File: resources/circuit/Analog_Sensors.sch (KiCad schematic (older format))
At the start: 43 parts, among them J3 Screw_Terminal_1x08, Q10 BSS138, Q11 BSS138, Q7 BSS138, Q8 BSS138, Q9 BSS138, U13 Airspeed, U14 Static Pressure, U15 MAP Pressure, U16 MCP3008, U8 MCP3008

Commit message: Schematic work
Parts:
- removed U16: MCP3008, SMD_Packages:SO-16-L, symbol MCP3008
- added U9: MCP3008, symbol MCP3008
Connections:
- net +5V: now also U9.15 (VREF), U9.16 (VDD)
- net ASI: now also U8.1 (CH0)
- net BARO: now also U8.2 (CH1)
- net CHT: now also U8.6 (CH5)
- net CurrentMeter: now also U8.7 (CH6)
- net GND: now also U9.14 (AGND), U9.9 (DGND)
- net MAP: now also U8.3 (CH2)
- net MCP0H: now also U8.10 (~CS~/SHDN)
- net MCP1H: now also U9.10 (~CS~/SHDN); no longer U8.10 (~CS~/SHDN)
- net MISOH: now also U9.12 (DOUT)
- net MOSIH: now also U9.11 (DIN)
- net OilPressure: now also U8.4 (CH3)
- net OilTemp: now also U8.5 (CH4)
- net SCLKH: now also U9.13 (CLK)
- net VoltageMeter: now also U8.8 (CH7)
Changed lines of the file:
@@
 +5V
 $Comp
-L GND #PWR033
+L GND #PWR032
 U 1 1 5914E423
 P 5800 4610
-F 0 "#PWR033" H 5800 4610 30  0001 C CNN
+F 0 "#PWR032" H 5800 4610 30  0001 C CNN
 F 1 "GND" H 5800 4540 30  0001 C CNN
 F 2 "" H 5800 4610 60  0000 C CNN
@@
 $EndComp
 $Comp
-L GND #PWR034
+L GND #PWR033
 U 1 1 5914E429
 P 5800 2460
-F 0 "#PWR034" H 5800 2460 30  0001 C CNN
+F 0 "#PWR033" H 5800 2460 30  0001 C CNN
 F 1 "GND" H 5800 2390 30  0001 C CNN
 F 2 "" H 5800 2460 60  0000 C CNN
@@
 Text Label 4750 1260 2    60   ~ 0
 CHT
-$Comp
-L MCP3008 U16
-U 1 1 5914E457
-P 5800 1610
-F 0 "U16" H 5350 2060 50  0000 C CNN
-F 1 "MCP3008" H 6150 2060 50  0000 C CNN
-F 2 "SMD_Packages:SO-16-L" H 5700 1510 50  0001 C CNN
-F 3 "" H 5800 1610 50  0001 C CNN
-	1    5800 1610
-	1    0    0    -1
-$EndComp
 Text Notes 4970 5070 0    157  Italic 31
 A/D Module
@@
 $EndComp
 $Comp
-L GND #PWR035
+L GND #PWR034
 U 1 1 59151DCA
 P 1580 1450
-F 0 "#PWR035" H 1580 1450 30  0001 C CNN
+F 0 "#PWR034" H 1580 1450 30  0001 C CNN
 F 1 "GND" H 1580 1380 30  0001 C CNN
 F 2 "" H 1580 1450 60  0001 C CNN
@@
 $EndComp
 $Comp
-L GND #PWR036
+L GND #PWR035
 U 1 1 59151DFB
 P 1580 2450
-F 0 "#PWR036" H 1580 2450 30  0001 C CNN
+F 0 "#PWR035" H 1580 2450 30  0001 C CNN
 F 1 "GND" H 1580 2380 30  0001 C CNN
 F 2 "" H 1580 2450 60  0001 C CNN
@@
 $EndComp
 $Comp
-L GND #PWR037
+L GND #PWR036
 U 1 1 59151E25
 P 1580 3450
-F 0 "#PWR037" H 1580 3450 30  0001 C CNN
+F 0 "#PWR036" H 1580 3450 30  0001 C CNN
 F 1 "GND" H 1580 3380 30  0001 C CNN
 F 2 "" H 1580 3450 60  0001 C CNN
@@
 NoConn ~ 1830 5720
 NoConn ~ 1830 5920
-$Comp
-L MCP3008 U8
-U 1 1 59151B46
-P 5800 3760
-F 0 "U8" H 5350 4210 50  0000 C CNN
-F 1 "MCP3008" H 6150 4210 50  0000 C CNN
-F 2 "" H 5700 3660 50  0001 C CNN
-F 3 "" H 5800 3760 50  0001 C CNN
-	1    5800 3760
-	1    0    0    -1
-$EndComp
 Text HLabel 1800 6650 2    60   Input ~ 0
 +5V
@@
 $EndComp
 $Comp
-L GND #PWR038
+L GND #PWR037
 U 1 1 5915DC2B
 P 5590 6120
-F 0 "#PWR038" H 5590 6120 30  0001 C CNN
+F 0 "#PWR037" H 5590 6120 30  0001 C CNN
 F 1 "GND" H 5590 6050 30  0001 C CNN
 F 2 "" H 5590 6120 60  0001 C CNN
@@
 Wire Wire Line
 	4930 2010 4930 2250
+$Comp
+L MCP3008 U8
+U 1 1 59157E17
+P 5800 1610
+F 0 "U8" H 5350 2060 50  0000 C CNN
+F 1 "MCP3008" H 6150 2060 50  0000 C CNN
+F 2 "" H 5700 1510 50  0001 C CNN
+F 3 "" H 5800 1610 50  0001 C CNN
+	1    5800 1610
+	1    0    0    -1
+$EndComp
+$Comp
+L MCP3008 U9
+U 1 1 591584A5
+P 5800 3760
+F 0 "U9" H 5350 4210 50  0000 C CNN
+F 1 "MCP3008" H 6150 4210 50  0000 C CNN
+F 2 "" H 5700 3660 50  0001 C CNN
+F 3 "" H 5800 3760 50  0001 C CNN
+	1    5800 3760
+	1    0    0    -1
+$EndComp
 $EndSCHEMATC

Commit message: Another RPM reading solution
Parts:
- added C14, C?: 22n, symbol C_Small
- added D?: Diode, Diodes_SMD:D_0603, symbol D_Small
- added R14, R?: 47k, symbol R_Small
- added R15, R?: 100, symbol R_Small
- added R18, R? (x2): 100k, Resistors_SMD:R_0603, symbol R_Small
- added R19, R? (x3): 10k, Resistors_SMD:R_0603, symbol R_Small
- added R20, R?: 220, Resistors_SMD:R_0603, symbol R_Small
- added U10, U?: LTV-817, Housings_DIP:DIP-4_W7.62mm, symbol LTV-817
- added U11, U? (x2): LM358, symbol LM358
- D7: value 3.3V -> 5.6V
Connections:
- net +3.3V: now also R15.2, R?.2
- net +5V: now also R18.2, R?.2, U11.8 (V+), U11.8 (V+), U?.8 (V+), U?.8 (V+)
- net GND: now also C14.2, C?.2, D?.2 (A), R19.1, R?.1, R?.1, U10.2, U10.3, U11.4 (V-), U11.4 (V-), U?.2, U?.3, U?.4 (V-), U?.4 (V-)
- net TACH: now also R15.1, R?.1, U10.4, U?.4; no longer D7.1 (K), R17.1
- net Tachometer: now also R?.2
- new net: D7.1 (K), R14.2, R17.1
- new net: C14.1, R14.1, U11.3 (+)
- new net: R20.2, U10.1
- new net: U11.1, U11.2 (-), U11.5 (+)
- new net: R18.1, R19.2, U11.6 (-)
- new net: R20.1, U11.7
- new net: R?.2, U?.1
- new net: U?.1, U?.2 (-), U?.3 (+)
- new net: C?.1, R?.1, U?.3 (+)
- new net: R?.1, U?.1
- new net: R?.1, R?.2, U?.2 (-)
- new net: D?.1 (K), R?.1, R?.2
- new net: R?.1, R?.2, R?.2
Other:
- note added: "Tachometer Module"
- note removed: "Tachymeter Module"
- moved on the sheet: D6, D7, J3, R16, R17, R47, R48, R49, U8, U9

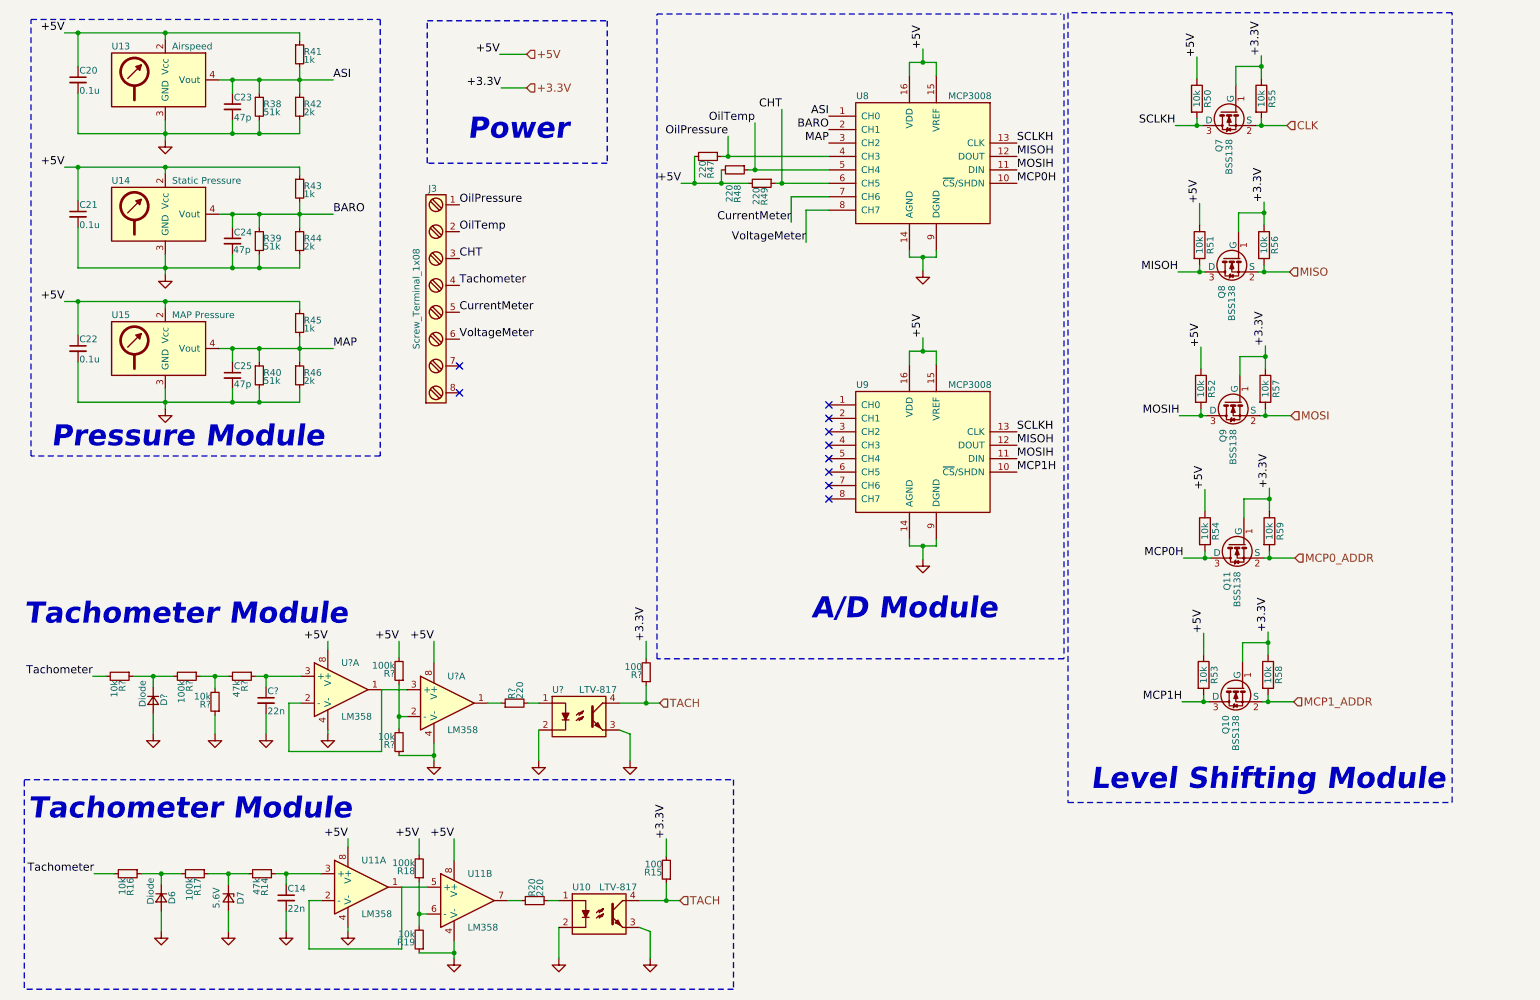
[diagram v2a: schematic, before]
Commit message: Clear PCB network + clean schematic
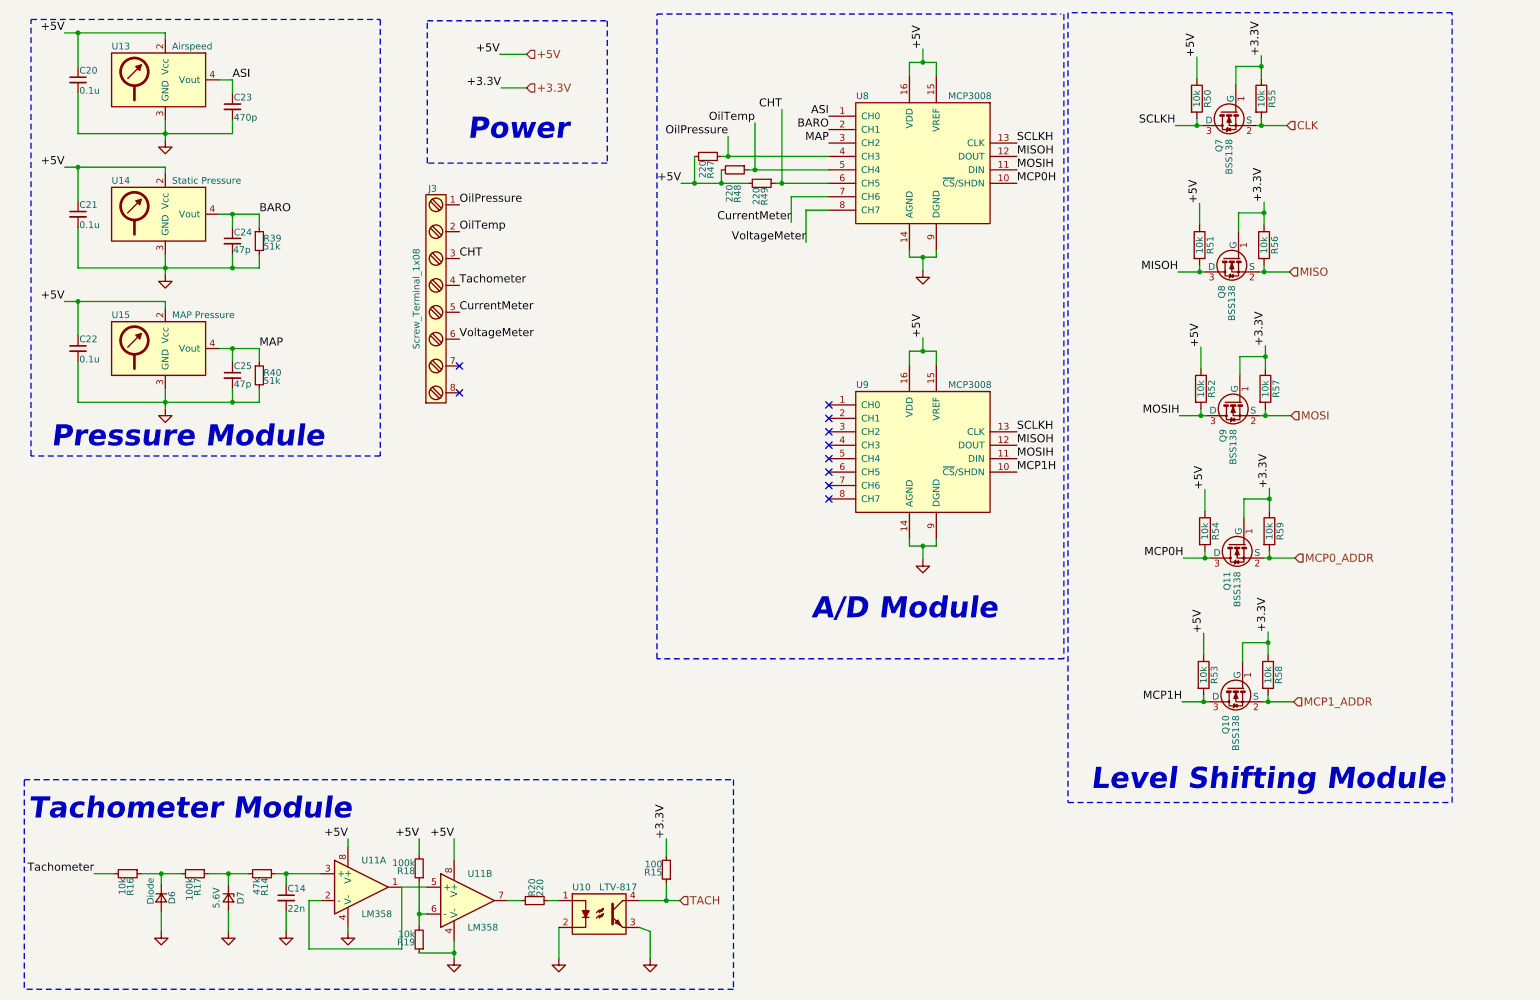
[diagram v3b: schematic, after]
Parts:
- removed C?: 22n, symbol C_Small
- removed D?: Diode, Diodes_SMD:D_0603, symbol D_Small
- removed R38: 51k, Capacitors_SMD:C_0603, symbol R_Small
- removed R41, R43, R45: 1k, Capacitors_SMD:C_0603, symbol R_Small
- removed R42, R44, R46: 2k, Capacitors_SMD:C_0603, symbol R_Small
- removed R?: 100, symbol R_Small
- removed R? (x2): 100k, Resistors_SMD:R_0603, symbol R_Small
- removed R? (x3): 10k, Resistors_SMD:R_0603, symbol R_Small
- removed R?: 220, Resistors_SMD:R_0603, symbol R_Small
- removed R?: 47k, symbol R_Small
- removed U?: LTV-817, Housings_DIP:DIP-4_W7.62mm, symbol LTV-817
- removed U? (x2): LM358, symbol LM358
- C14: footprint (none) -> Capacitors_SMD:C_0603
- C23: value 47p -> 470p
- J3: footprint (none) -> Connectors_Terminal_Blocks:TerminalBlock_Pheonix_MPT-2.54mm_8pol
- R14, R15, R50, R51, R52, R53, R54, R55, R56, R57, R58, R59: footprint (none) -> Resistors_SMD:R_0603
- R39, R40, R47, R48, R49: footprint Capacitors_SMD:C_0603 -> Resistors_SMD:R_0603
- U11: footprint (none) -> Housings_SOIC:SOIC-8_3.9x4.9mm_Pitch1.27mm
- U8, U9: footprint (none) -> Housings_SOIC:SOIC-16_3.9x9.9mm_Pitch1.27mm

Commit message: Work on circuit & PCB
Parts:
- removed C20, C21, C22: 0.1u, Capacitors_SMD:C_0603, symbol C_Small
- removed C23: 470p, Capacitors_SMD:C_0603, symbol C_Small
- removed C24, C25: 47p, Capacitors_SMD:C_0603, symbol C_Small
- removed J3: Screw_Terminal_1x08, Connectors_Terminal_Blocks:TerminalBlock_Pheonix_MPT-2.54mm_8pol, symbol Screw_Terminal_1x08
- removed Q10, Q11, Q7, Q9: BSS138, TO_SOT_Packages_SMD:SOT-23, symbol BSS138
- removed R15: 100, Resistors_SMD:R_0603, symbol R_Small
- removed R20, R47, R48, R49: 220, Resistors_SMD:R_0603, symbol R_Small
- removed R39, R40: 51k, Resistors_SMD:R_0603, symbol R_Small
- removed R50, R52, R53, R54, R55, R57, R58, R59: 10k, Resistors_SMD:R_0603, symbol R
- removed U10: LTV-817, Housings_DIP:DIP-4_W7.62mm, symbol LTV-817
- removed U13: Airspeed, SMD_Packages:SOIC-8-N, symbol MPXV5004DP
- removed U14: Static Pressure, SMD_Packages:SOIC-8-N, symbol MPXA6115A
- removed U15: MAP Pressure, SMD_Packages:SOIC-8-N, symbol MPXA6115A
- removed U8, U9: MCP3008, Housings_SOIC:SOIC-16_3.9x9.9mm_Pitch1.27mm, symbol MCP3008
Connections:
- net MISO is gone; now on net TACH: Q8.2 (S), R56.2
- net MISOH is gone; now on an unnamed net: Q8.3 (D), R51.2
- no-connect marks 10 -> 0
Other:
- note removed: "A/D Module"
- note removed: "Level Shifting Module"
- note removed: "Pressure Module"
- moved on the sheet: Q8, R51, R56
